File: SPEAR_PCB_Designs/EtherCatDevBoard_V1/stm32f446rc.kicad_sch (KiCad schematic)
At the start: 39 parts, among them J1 USB_C_Receptacle_USB2.0_16P, J2 FTSH-107-01-F-DV-K-P-TR, J3 Conn_01x21_Pin, J4 Conn_01x21_Pin, SW1 SW_Push, U1 USBLC6-2SC6, U2 STM32F446RCT6, U3 AMS1117-3.3, U6 TPS2116DRL, Y1 16MHz

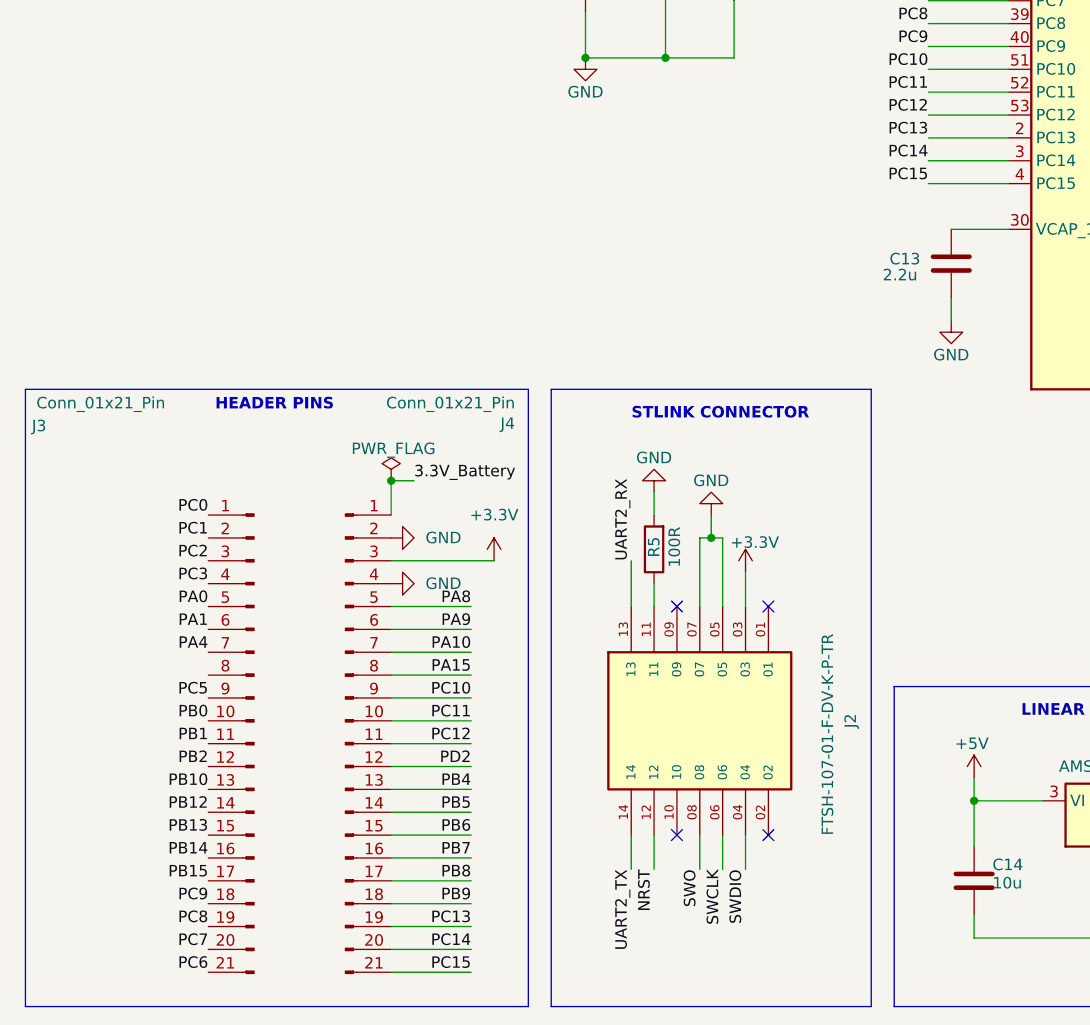
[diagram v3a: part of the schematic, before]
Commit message: Continued work on EtherCAT microcontroller dev board. Updated it's head pinout.
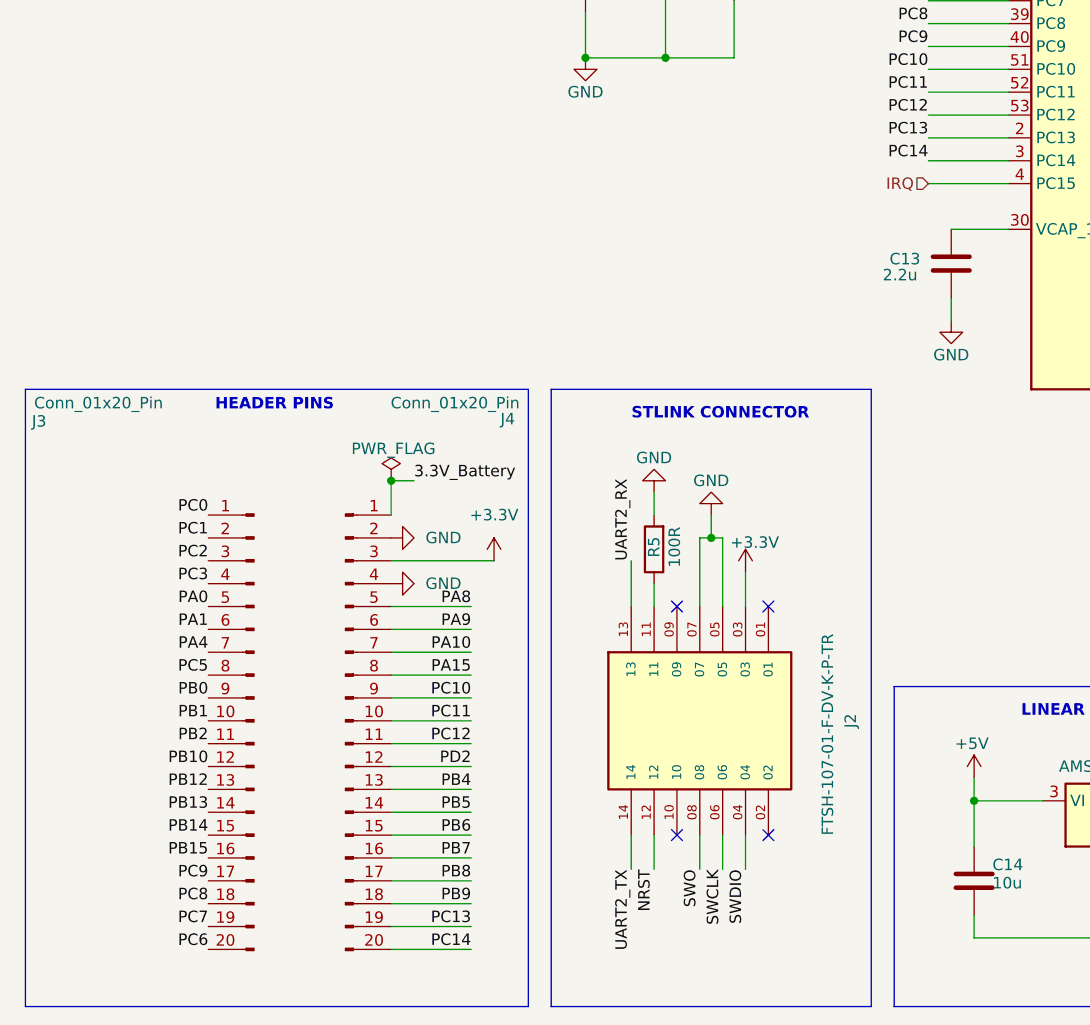
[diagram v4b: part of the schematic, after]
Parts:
- J3, J4: value Conn_01x21_Pin -> Conn_01x20_Pin; footprint Connector_PinHeader_2.54mm:PinHeader_1x21_P2.54mm_Vertical -> Connector_PinHeader_2.54mm:PinHeader_1x20_P2.54mm_Vertical; symbol Connector:Conn_01x21_Pin -> Connector:Conn_01x20_Pin
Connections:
- net PB0: now also J3.9 (Pin_9); no longer J3.10 (Pin_10)
- net PB1: now also J3.10 (Pin_10); no longer J3.11 (Pin_11)
- net PB10: now also J3.12 (Pin_12); no longer J3.13 (Pin_13)
- net PB12: now also J3.13 (Pin_13); no longer J3.14 (Pin_14)
- net PB13: now also J3.14 (Pin_14); no longer J3.15 (Pin_15)
- net PB14: now also J3.15 (Pin_15); no longer J3.16 (Pin_16)
- net PB15: now also J3.16 (Pin_16); no longer J3.17 (Pin_17)
- net PB2: now also J3.11 (Pin_11); no longer J3.12 (Pin_12)
- net PC5: now also J3.8 (Pin_8); no longer J3.9 (Pin_9)
- net PC6: now also J3.20 (Pin_20); no longer J3.21 (Pin_21)
- net PC7: now also J3.19 (Pin_19); no longer J3.20 (Pin_20)
- net PC8: now also J3.18 (Pin_18); no longer J3.19 (Pin_19)
- net PC9: now also J3.17 (Pin_17); no longer J3.18 (Pin_18)
- net PC15 renamed IRQ
- net IRQ: no longer J4.21 (Pin_21)

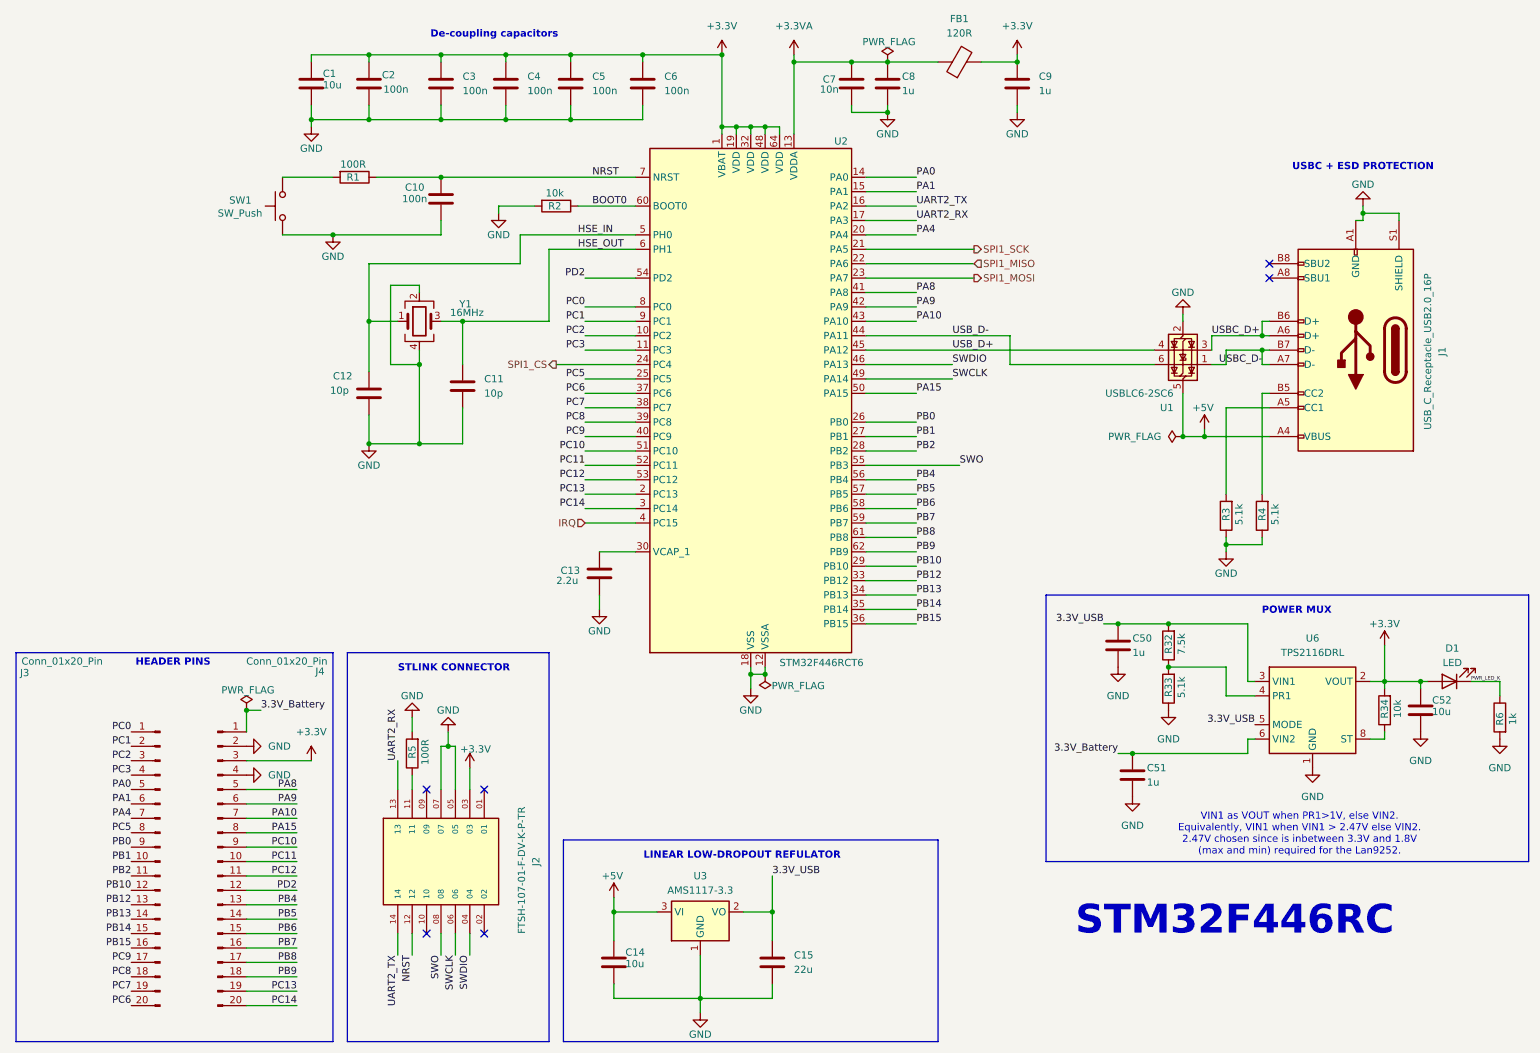
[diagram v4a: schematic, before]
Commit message: Started adding digikey part ID's to the EtherCAT microcontroller dev. board, but incomplete as of now.
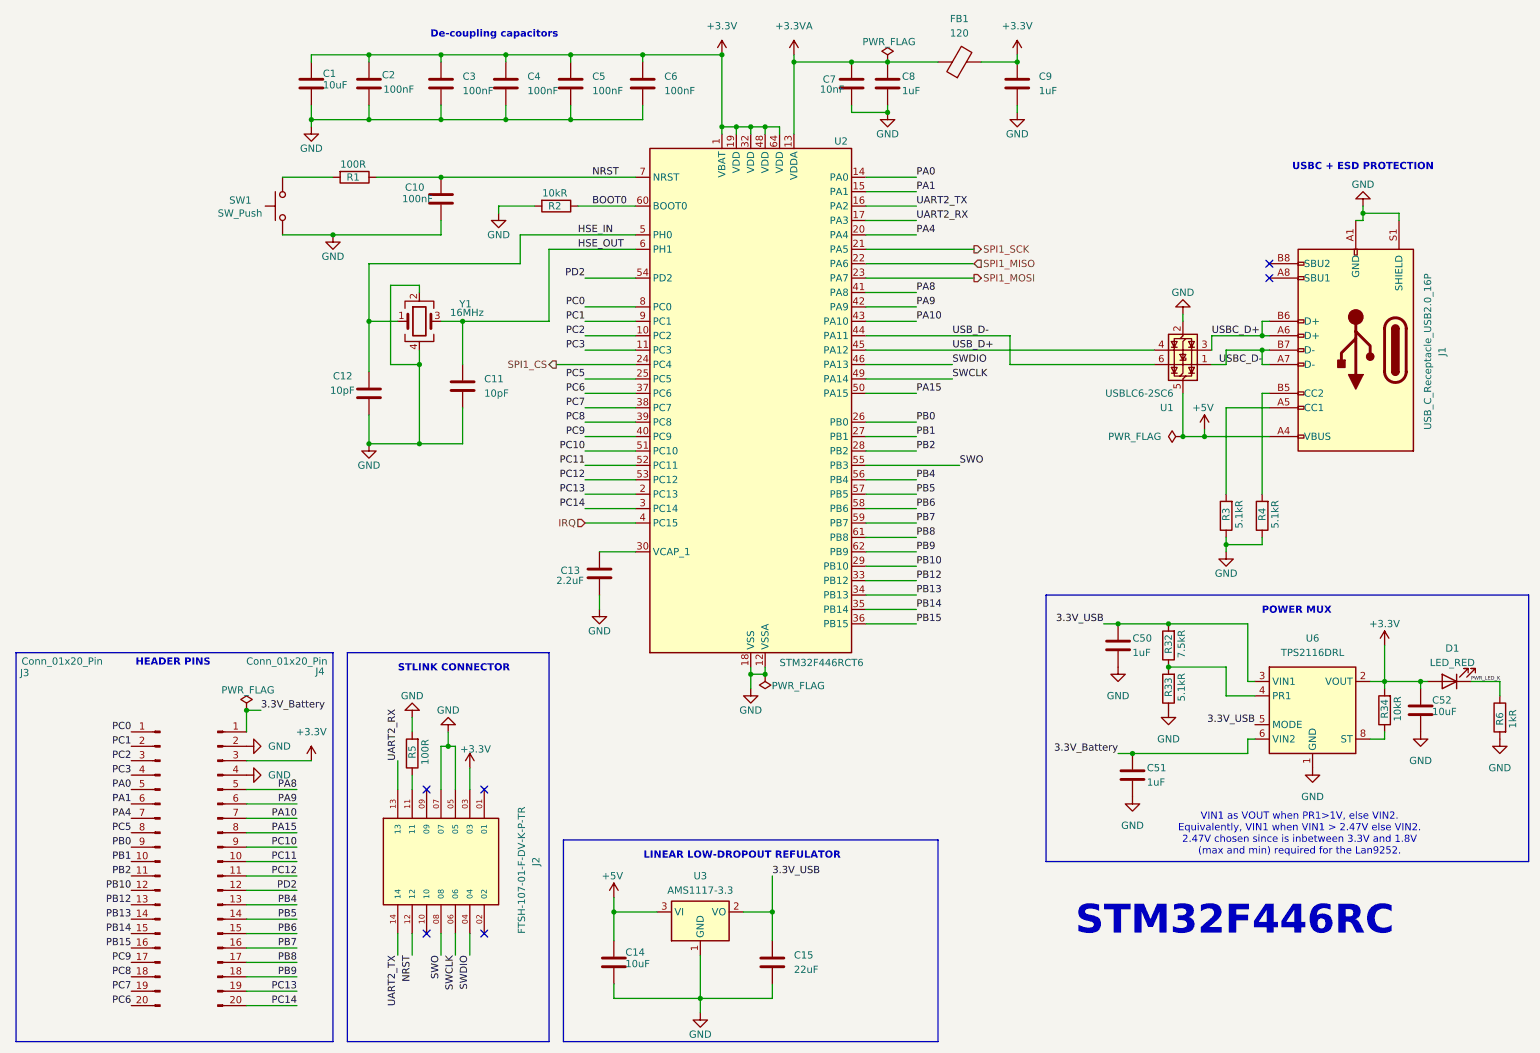
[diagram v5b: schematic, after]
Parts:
- C1, C14, C52: value 10u -> 10uF; DigiKey_Part_Number (none) -> 1276-1192-1-ND
- C10, C2, C3, C4, C5, C6: value 100n -> 100nF; DigiKey_Part_Number (none) -> 1276-1043-1-ND
- C11, C12: value 10p -> 10pF; DigiKey_Part_Number (none) -> 1276-1139-1-ND
- C13: value 2.2u -> 2.2uF; DigiKey_Part_Number (none) -> 1276-1108-1-ND
- C15: value 22u -> 22uF; DigiKey_Part_Number (none) -> 1276-CL21A226MAYNNNECT-ND
- C50, C51, C8, C9: value 1u -> 1uF; DigiKey_Part_Number (none) -> 1276-1067-1-ND
- C7: value 10n -> 10nF; DigiKey_Part_Number (none) -> 1276-1051-1-ND
- D1: value LED -> LED_RED; DigiKey_Part_Number (none) -> 732-12015-1-ND
- FB1: value 120R -> 120
- R1, R5: DigiKey_Part_Number (none) -> 311-100LRCT-ND
- R2, R34: value 10k -> 10kR; DigiKey_Part_Number (none) -> 311-10KJRCT-ND
- R3, R33, R4: value 5.1k -> 5.1kR; DigiKey_Part_Number (none) -> 311-5.10KLRCT-ND
- R32: value 7.5k -> 7.5kR; DigiKey_Part_Number (none) -> 311-7.50KLRCT-ND
- R6: value 1k -> 1kR; DigiKey_Part_Number (none) -> 311-1.0KJRCT-ND

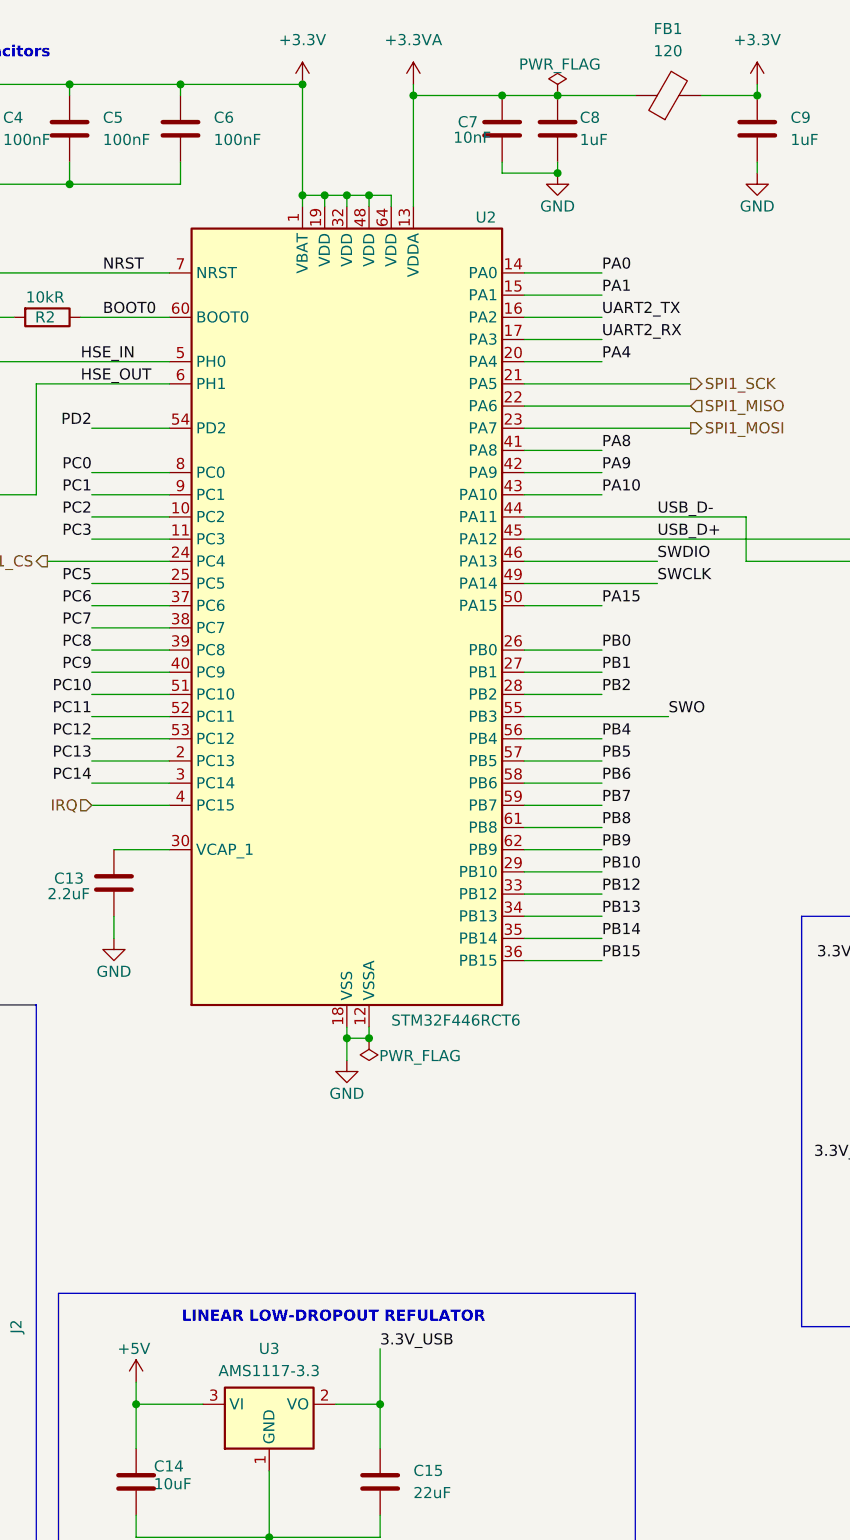
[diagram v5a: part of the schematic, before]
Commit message: Finished etherCAT microcontroller dev board component selection. BOM is available. PCB layout incomplete.
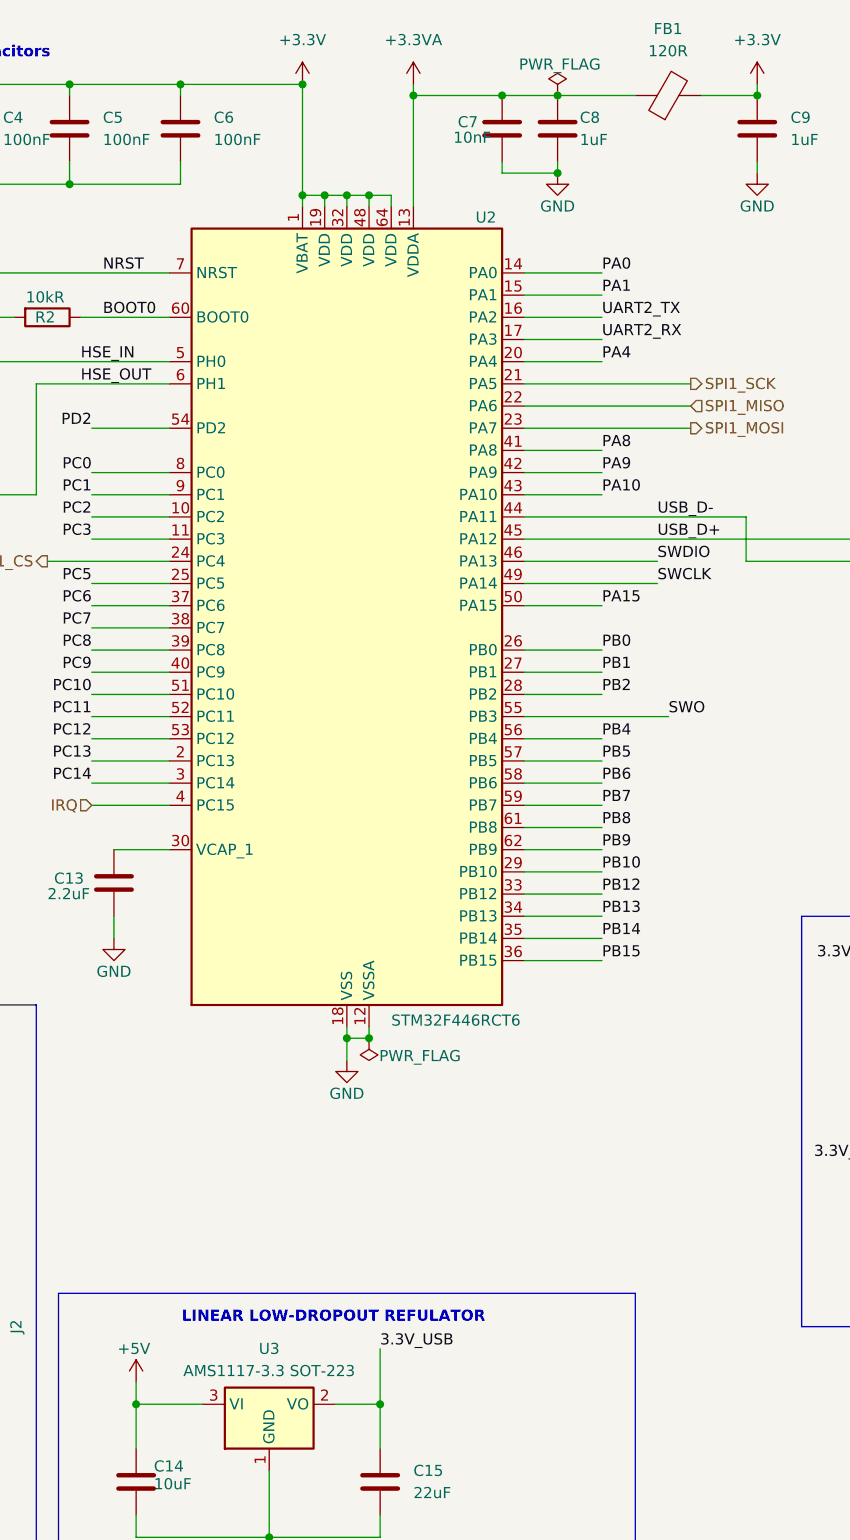
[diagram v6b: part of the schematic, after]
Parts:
- FB1: value 120 -> 120R; DigiKey_Part_Number (none) -> 490-5254-1-ND
- J1: DigiKey_Part_Number (none) -> 2073-USB4105-GF-A-120CT-ND
- J3, J4: DigiKey_Part_Number (none) -> 2057-PH1-20-UA-ND
- SW1: DigiKey_Part_Number (none) -> CKN12322-1-ND
- U1: DigiKey_Part_Number (none) -> 497-5235-1-ND
- U2: DigiKey_Part_Number (none) -> 497-17472-ND
- U3: value AMS1117-3.3 -> AMS1117-3.3 SOT-223; DigiKey_Part_Number (none) -> 5399-AMS1117-3.3SOT-223CT-ND
- U6: DigiKey_Part_Number (none) -> 296-TPS2116DRLRCT-ND
- Y1: DigiKey_Part_Number (none) -> 2151-R2520-16.000-10-1020-EXT-TRCT-ND
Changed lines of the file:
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@@
 			)
 		)
+		(property "DigiKey_Part_Number" "497-17472-ND"
+			(at 143.51 83.82 0)
+			(effects
+				(font
+					(size 1.27 1.27)
+				)
+				(hide yes)
+			)
+		)
 		(pin "1"
 		)
@@
 			)
 		)
+		(property "DigiKey_Part_Number" "296-TPS2116DRLRCT-ND"
+			(at 242.57 137.16 0)
+			(effects
+				(font
+					(size 1.27 1.27)
+				)
+				(hide yes)
+			)
+		)
 		(pin "6"
 		)
@@
 			)
 		)
+		(property "DigiKey_Part_Number" "2057-PH1-20-UA-ND"
+			(at 39.37 163.83 0)
+			(effects
+				(font
+					(size 1.27 1.27)
+				)
+				(hide yes)
+			)
+		)
 		(pin "6"
 		)
@@
 			)
 		)
-		(property "Value" "AMS1117-3.3"
+		(property "Value" "AMS1117-3.3 SOT-223"
 			(at 134.62 168.91 0)
 			(effects
@@
 			)
 		)
+		(property "DigiKey_Part_Number" "5399-AMS1117-3.3SOT-223CT-ND"
+			(at 134.62 172.72 0)
+			(effects
+				(font
+					(size 1.27 1.27)
+				)
+				(hide yes)
+			)
+		)
 		(pin "2"
 		)
@@
 			)
 		)
+		(property "DigiKey_Part_Number" "497-5235-1-ND"
+			(at 219.71 76.2 0)
+			(effects
+				(font
+					(size 1.27 1.27)
+				)
+				(hide yes)
+			)
+		)
 		(pin "3"
 		)
@@
 			)
 		)
+		(property "DigiKey_Part_Number" "2057-PH1-20-UA-ND"
+			(at 49.53 163.83 0)
+			(effects
+				(font
+					(size 1.27 1.27)
+				)
+				(hide yes)
+			)
+		)
 		(pin "6"
 		)
@@
 			)
 		)
+		(property "DigiKey_Part_Number" "CKN12322-1-ND"
+			(at 60.96 48.26 90)
+			(effects
+				(font
+					(size 1.27 1.27)
+				)
+				(hide yes)
+			)
+		)
 		(pin "2"
 		)
@@
 			)
 		)
-		(property "Value" "120"
+		(property "Value" "120R"
 			(at 180.2892 17.78 90)
 			(effects
@@
 			)
 		)
+		(property "DigiKey_Part_Number" "490-5254-1-ND"
+			(at 180.34 22.86 90)
+			(effects
+				(font
+					(size 1.27 1.27)
+				)
+				(hide yes)
+			)
+		)
 		(pin "2"
 		)
@@
 			)
 		)
+		(property "DigiKey_Part_Number" "2073-USB4105-GF-A-120CT-ND"
+			(at 250.19 73.66 90)
+			(effects
+				(font
+					(size 1.27 1.27)
+				)
+				(hide yes)
+			)
+		)
 		(pin "S1"
 		)
@@
 			(at 85.09 68.58 0)
 			(effects
+				(font
+					(size 1.27 1.27)
+				)
+				(hide yes)
+			)
+		)
+		(property "DigiKey_Part_Number" "2151-R2520-16.000-10-1020-EXT-TRCT-ND"
+			(at 85.09 68.58 0)
+			(effects

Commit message: Continued work on the Ethercat dev board. Unfinished.
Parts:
- J1: footprint Connector_USB:USB_C_Receptacle_GCT_USB4105-xx-A_16P_TopMnt_Horizontal -> LAN9252 Footprints:USB_C_Receptacle_GCT_USB4105-xx-A_16P_TopMnt_Horizontal
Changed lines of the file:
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@@
 			)
 		)
-		(property "Footprint" "Connector_USB:USB_C_Receptacle_GCT_USB4105-xx-A_16P_TopMnt_Horizontal"
+		(property "Footprint" "LAN9252 Footprints:USB_C_Receptacle_GCT_USB4105-xx-A_16P_TopMnt_Horizontal"
 			(at 246.38 73.66 0)
 			(effects
